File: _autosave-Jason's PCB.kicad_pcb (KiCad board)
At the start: 2 copper layers, 66.7 x 85.7 mm, 11 parts, among them U1 Elite-C

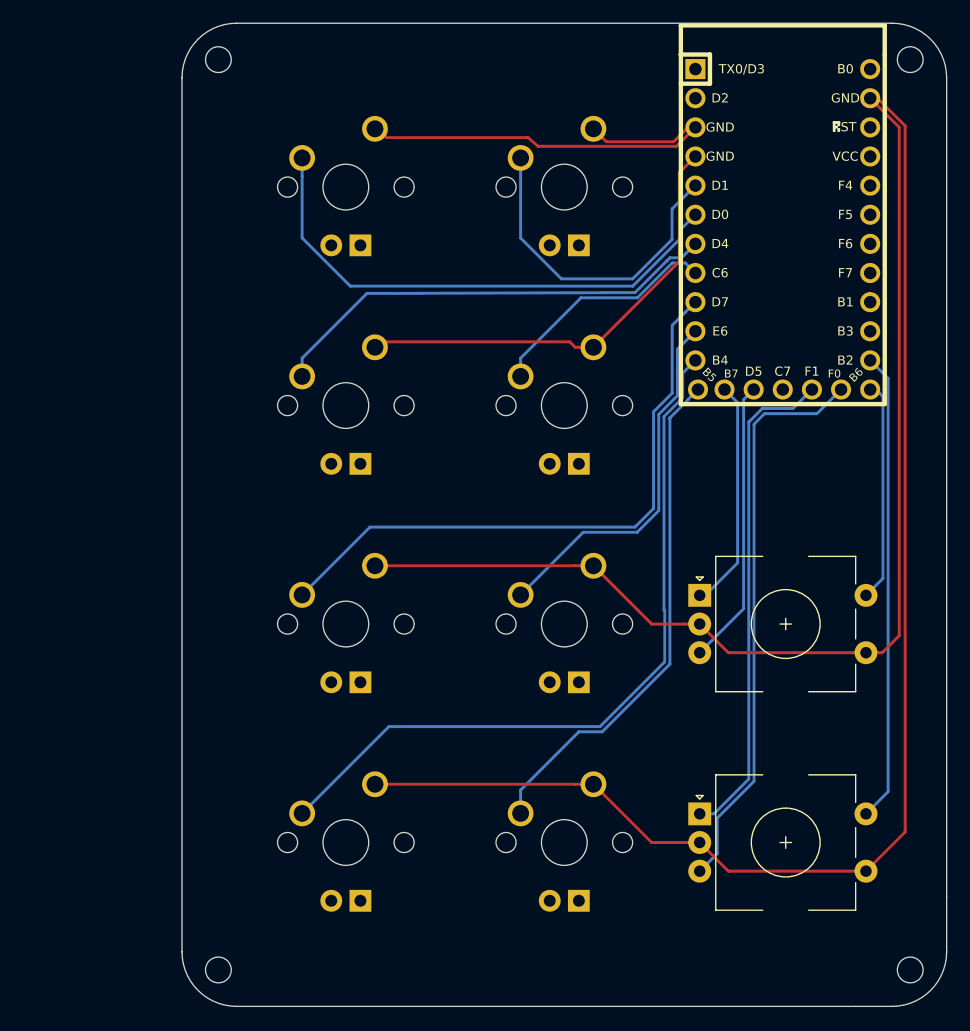
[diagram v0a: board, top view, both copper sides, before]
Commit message: Routing
-Changed nets in schematic to make routing easier
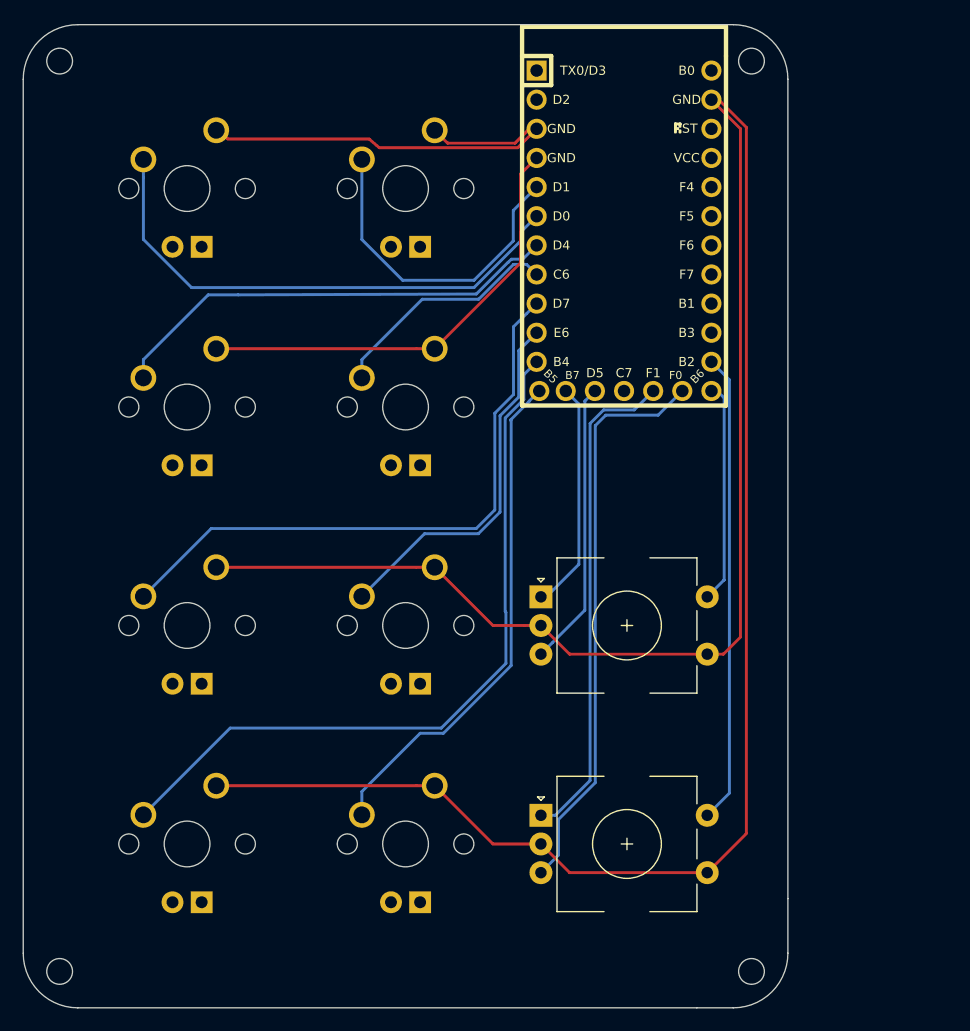
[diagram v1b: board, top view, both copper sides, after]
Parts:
- moved U1 13.8 mm to (138.6, 38.7)
- moved SW_A1 13.8 mm to (100.5, 35.1)
- moved SW_B1 13.8 mm to (100.5, 54.1)
- moved SW_C1 13.8 mm to (100.5, 73.2)
- moved SW_D1 13.8 mm to (100.5, 92.2)
- moved SW_A2 13.8 mm to (119.5, 35.1)
- moved SW_B2 13.8 mm to (119.5, 54.1)
- moved SW_C2 13.8 mm to (119.5, 73.2)
- moved SW_D2 13.8 mm to (119.5, 92.2)
- moved SW_E1 13.8 mm to (138.8, 73.2)
- moved SW_E2 13.8 mm to (138.8, 92.2)
